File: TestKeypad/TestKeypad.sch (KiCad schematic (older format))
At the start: 71 parts, among them J1 Mini-DIN-6, Q1 BS170, SW1 SW_SPST, SW10 SW_SPST, SW11 SW_SPST, SW12 SW_SPST, SW13 SW_SPST, SW14 SW_SPST, SW15 SW_SPST, SW16 SW_SPST, SW2 SW_SPST, SW3 SW_SPST, SW4 SW_SPST, SW5 SW_SPST, SW6 SW_SPST, SW7 SW_SPST, SW8 SW_SPST, SW9 SW_SPST, U1 ATtiny24A-PU

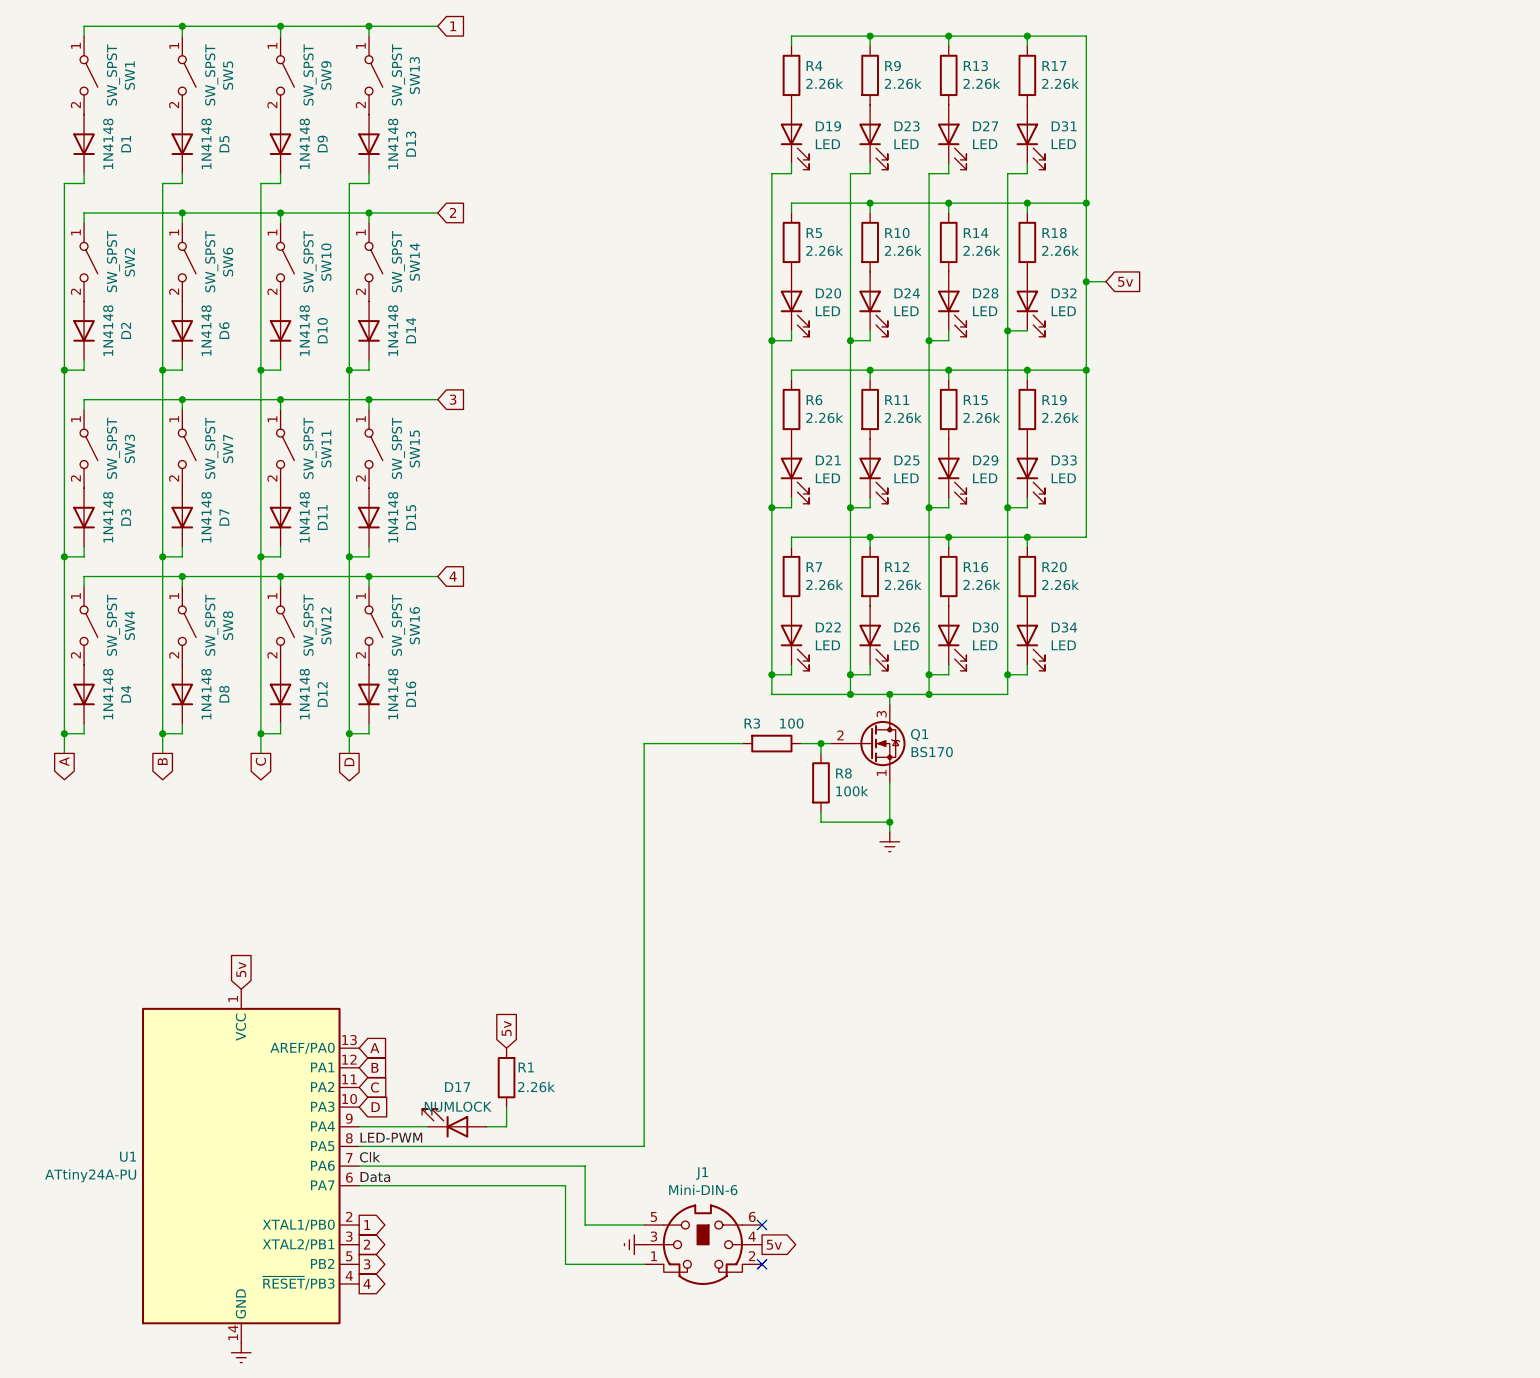
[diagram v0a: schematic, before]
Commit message: Revise test keypad to r02
Updated components to match the actual board and revised PCB layout
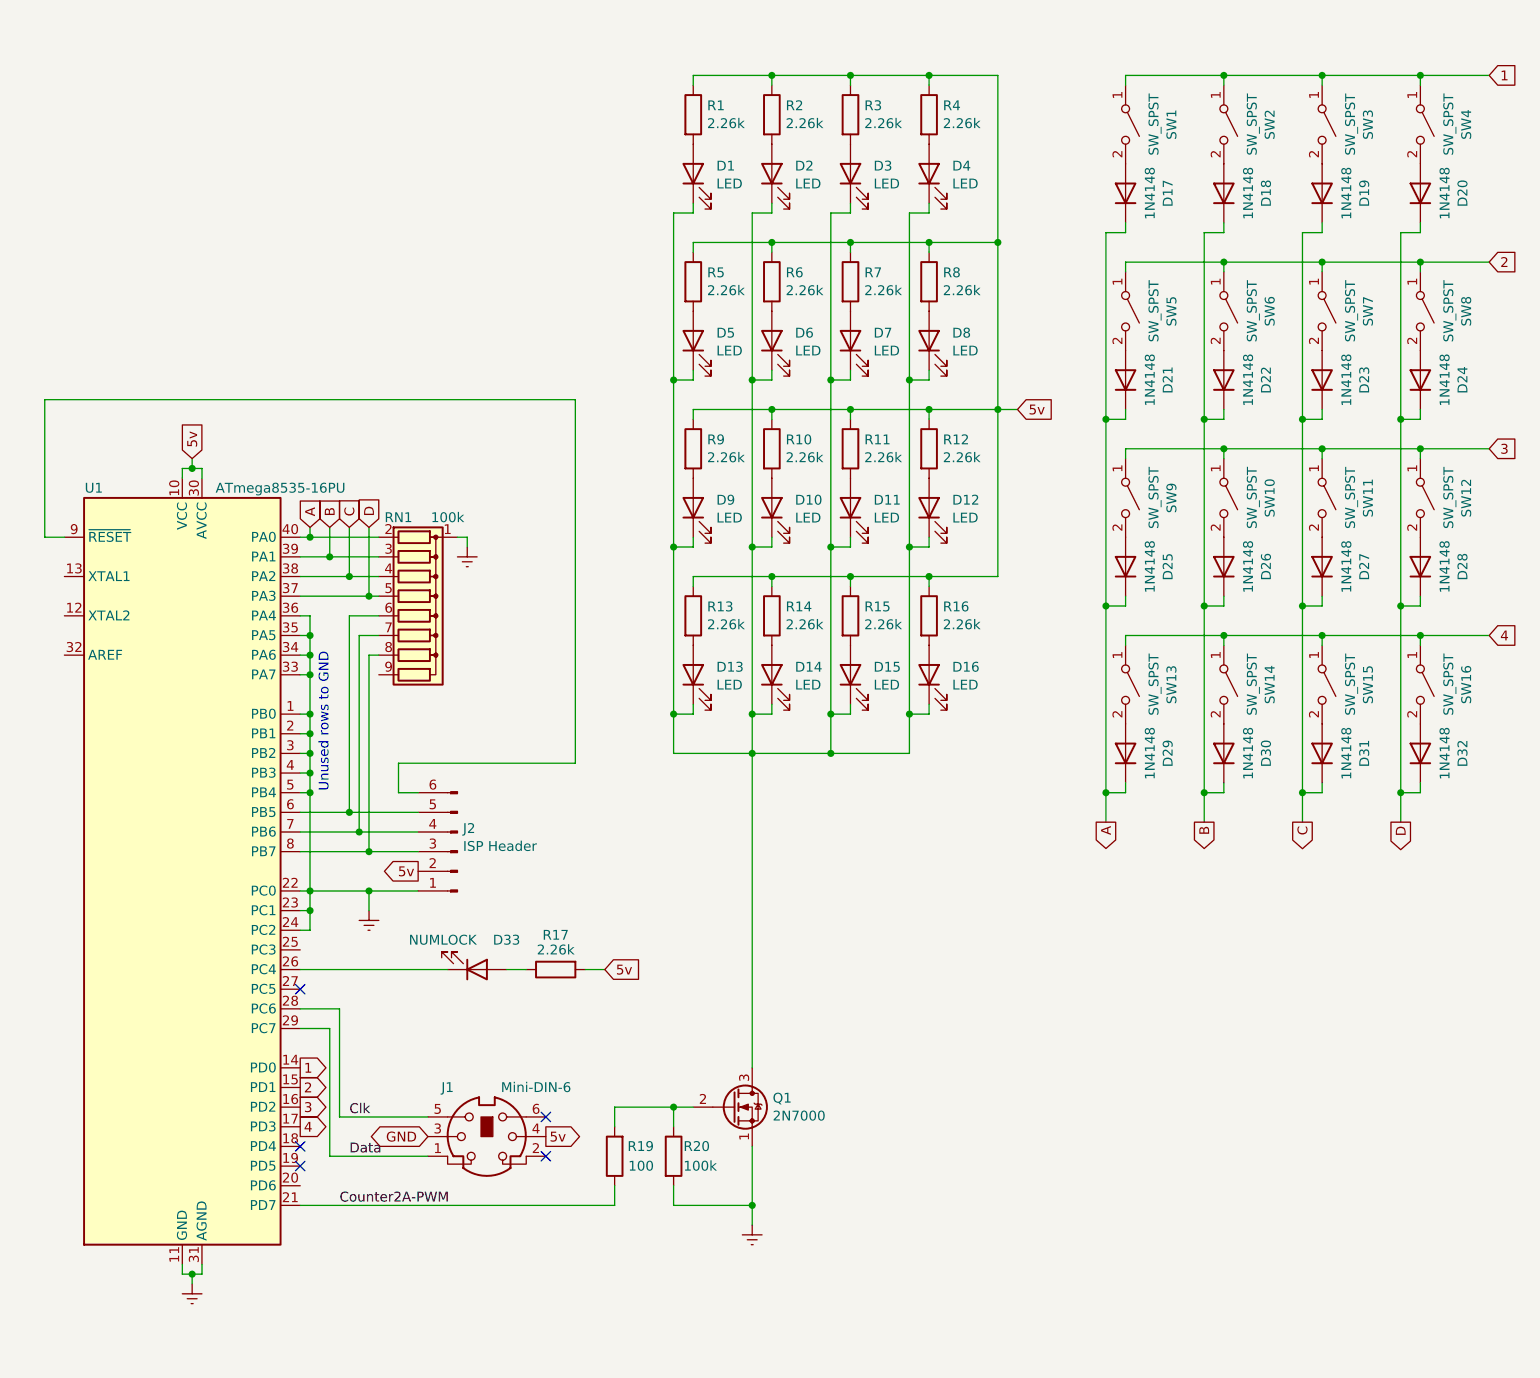
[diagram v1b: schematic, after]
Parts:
- removed D1, D10, D11, D12, D13, D14, D15, D16, D2, D3, D4, D5, D6, D7, D8, D9: 1N4148, Diode_SMD:D_MiniMELF_Handsoldering, symbol Device:D
- removed D17: NUMLOCK, MyOwnKeyboard:158301250, symbol Device:LED
- removed D19, D20, D21, D22, D23, D24, D25, D26, D27, D28, D29, D30, D31, D32, D34: LED, MyOwnKeyboard:158301250, symbol Device:LED
- removed R18: 2.26k, Resistor_SMD:R_0805_2012Metric_Pad1.15x1.40mm_HandSolder, symbol Device:R
- removed U1: ATtiny24A-PU, Package_DIP:DIP-14_W7.62mm_Socket, symbol MCU_Microchip_ATtiny:ATtiny24A-PU
- added D1, D10, D11, D12, D13, D14, D15, D16, D2, D3, D4, D5, D6, D7, D8, D9: LED, MyOwnKeyboard:158301250, symbol Device:LED
- added D17, D18, D19, D20, D21, D22, D23, D24, D25, D26, D27, D28, D29, D30, D31, D32: 1N4148, Diode_SMD:D_MiniMELF_Handsoldering, symbol Device:D
- added J2: ISP Header, Connector_PinHeader_2.54mm:PinHeader_2x03_P2.54mm_Vertical, symbol Connector:Conn_01x06_Male
- added R2: 2.26k, Resistor_SMD:R_0805_2012Metric_Pad1.15x1.40mm_HandSolder, symbol Device:R
- added RN1: 100k, Resistor_THT:R_Array_SIP9, symbol Device:R_Network08
- added U1: ATmega8535-16PU, Package_DIP:DIP-40_W15.24mm_Socket, symbol MCU_Microchip_ATmega:ATmega8535-16PU
- D33: value LED -> NUMLOCK
- Q1: value BS170 -> 2N7000
- R19: value 2.26k -> 100
- R20: value 2.26k -> 100k
- R3: value 100 -> 2.26k
- R8: value 100k -> 2.26k
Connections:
- net 1: now also SW2.1 (A), SW3.1 (A), SW4.1 (A), U1.14 (PD0); no longer SW13.1 (A), SW5.1 (A), SW9.1 (A)
- net 2: now also SW5.1 (A), SW7.1 (A), SW8.1 (A), U1.15 (PD1); no longer SW10.1 (A), SW14.1 (A), SW2.1 (A)
- net 3: now also SW10.1 (A), SW12.1 (A), SW9.1 (A), U1.16 (PD2); no longer SW15.1 (A), SW3.1 (A), SW7.1 (A)
- net 4: now also SW13.1 (A), SW14.1 (A), SW15.1 (A), U1.17 (PD3); no longer SW12.1 (A), SW4.1 (A), SW8.1 (A)
- net 5v: now also R1.1, R17.2, R3.1, R8.1, J2.2 (Pin_2), R2.1, U1.10 (VCC), U1.30 (AVCC); no longer R1.2, R17.1, R19.1, R20.1
- net A: now also D17.1 (K), D21.1 (K), D25.1 (K), D29.1 (K), RN1.2 (R1), U1.40 (PA0)
- net B: now also D18.1 (K), D22.1 (K), D26.1 (K), D30.1 (K), RN1.3 (R2), U1.39 (PA1)
- net C: now also D19.1 (K), D23.1 (K), D27.1 (K), D31.1 (K), RN1.4 (R3), U1.38 (PA2)
- net Clk: now also U1.28 (PC6)
- net D: now also D20.1 (K), D24.1 (K), D28.1 (K), D32.1 (K), RN1.5 (R4), U1.37 (PA3)
- net Data: now also U1.29 (PC7)
- net Earth: now also R20.2, J2.1 (Pin_1), RN1.1 (common), U1.1 (PB0), U1.11 (GND), U1.2 (PB1), U1.22 (PC0), U1.23 (PC1), U1.24 (PC2), U1.3 (PB2), U1.31 (AGND), U1.33 (PA7), U1.34 (PA6), U1.35 (PA5), U1.36 (PA4), U1.4 (PB3), U1.5 (PB4); no longer J1.3, R8.2
- net at SW14.2 (B): now also D30.2 (A)
- net at SW13.2 (B): now also D29.2 (A)
- net at SW15.2 (B): now also D31.2 (A)
- net at SW12.2 (B): now also D28.2 (A)
- net at SW8.2 (B): now also D24.2 (A)
- net at SW4.2 (B): now also D20.2 (A)
- net at SW16.2 (B): now also D32.2 (A)
- net at D33.1 (K): now also U1.26 (PC4); no longer Q1.3 (D)
- net at SW10.2 (B): now also D26.2 (A)
- net at SW9.2 (B): now also D25.2 (A)
- net at SW6.2 (B): now also D22.2 (A)
- net at SW5.2 (B): now also D21.2 (A)
- net at SW2.2 (B): now also D18.2 (A)
- net at SW1.2 (B): now also D17.2 (A)
- net at R14.2: now also D14.2 (A)
- net at R13.2: now also D13.2 (A)
- net at R10.2: now also D10.2 (A)
- net at R9.2: now also D9.2 (A)
- net at R5.2: now also D5.2 (A)
- net at R4.2: now also D4.2 (A)
- net at SW11.2 (B): now also D27.2 (A)
- net at SW7.2 (B): now also D23.2 (A)
- net at SW3.2 (B): now also D19.2 (A)
- net at R15.2: now also D15.2 (A)
- net at R11.2: now also D11.2 (A)
- net at R6.2: now also D6.2 (A)
- net at D33.2 (A): now also R17.1; no longer R19.2
- net at R16.2: now also D16.2 (A)
- net at R12.2: now also D12.2 (A)
- net at R7.2: now also D7.2 (A)
- net LED-PWM: no longer names the net of R3.2
- net LED-PWM: now also D3.2 (A)
- new net: D1.1 (K), D10.1 (K), D11.1 (K), D12.1 (K), D13.1 (K), D14.1 (K), D15.1 (K), D16.1 (K), D2.1 (K), D3.1 (K), D4.1 (K), D5.1 (K), D6.1 (K), D7.1 (K), D8.1 (K), D9.1 (K), Q1.3 (D)
- new net: D1.2 (A), R1.2
- new net: D2.2 (A), R2.2
- new net: D8.2 (A), R8.2
- new net: Q1.2 (G), R19.2, R20.1
- new net: J2.5 (Pin_5), RN1.6 (R5), U1.6 (PB5)
- new net: J2.4 (Pin_4), RN1.7 (R6), U1.7 (PB6)
- new net: J2.3 (Pin_3), RN1.8 (R7), U1.8 (PB7)
- new net: J2.6 (Pin_6), U1.9 (~RESET)
- new net Counter2A-PWM: R19.1, U1.21 (PD7)
- new net GND: J1.3
- no-connect marks 2 -> 5
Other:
- note added: "Unused rows to GND"

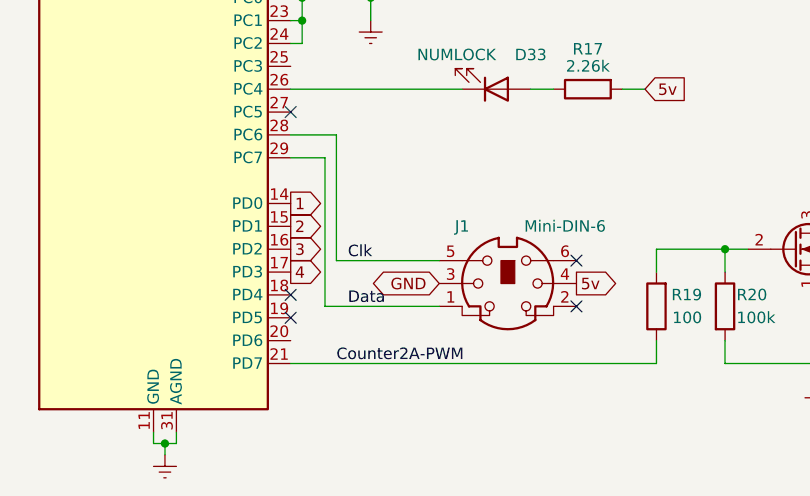
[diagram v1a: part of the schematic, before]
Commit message: Revise test keypad to r03
Tweaked just before making a production run
Added screw holes
Added an ISP header
Added pulldown resistor array to switch input lines
Also remapped an incorrectly-placed "GND" label to the actual ground net (which slipped through into the production run)
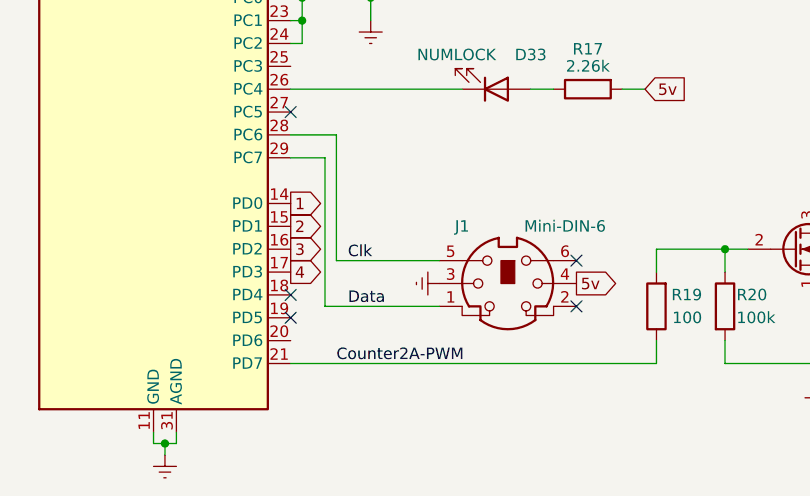
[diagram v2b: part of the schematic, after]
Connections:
- net GND is gone; now on net Earth: J1.3
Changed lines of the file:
@@
 	-1   0    0    -1
 $EndComp
-Text GLabel 2550 6300 0    50   BiDi ~ 0
-GND
 NoConn ~ 3150 6400
 NoConn ~ 3150 6200
@@
 Wire Wire Line
 	3350 5450 3450 5450
+$Comp
+L power:Earth #PWR?
+U 1 1 5F265FB5
+P 2550 6300
+F 0 "#PWR?" H 2550 6050 50  0001 C CNN
+F 1 "Earth" H 2550 6150 50  0001 C CNN
+F 2 "" H 2550 6300 50  0001 C CNN
+F 3 "~" H 2550 6300 50  0001 C CNN
+	1    2550 6300
+	0    1    1    0
+$EndComp
 $EndSCHEMATC
